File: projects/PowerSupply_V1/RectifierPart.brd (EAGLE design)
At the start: 80 x 45 mm, 12 parts, among them X1 IN, X2 PRI, X3 SEC, X4 OUT

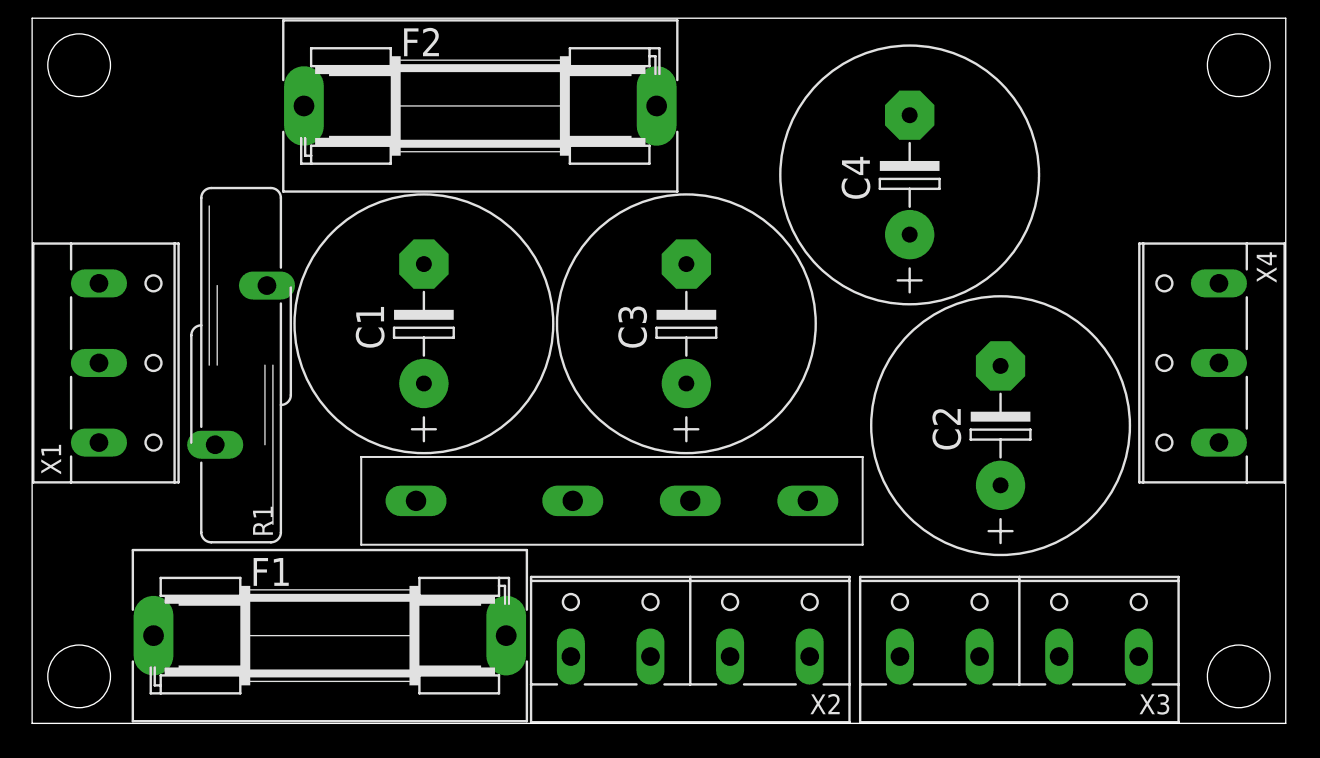
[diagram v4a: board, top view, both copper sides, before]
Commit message: feat: rectifier part routing finished
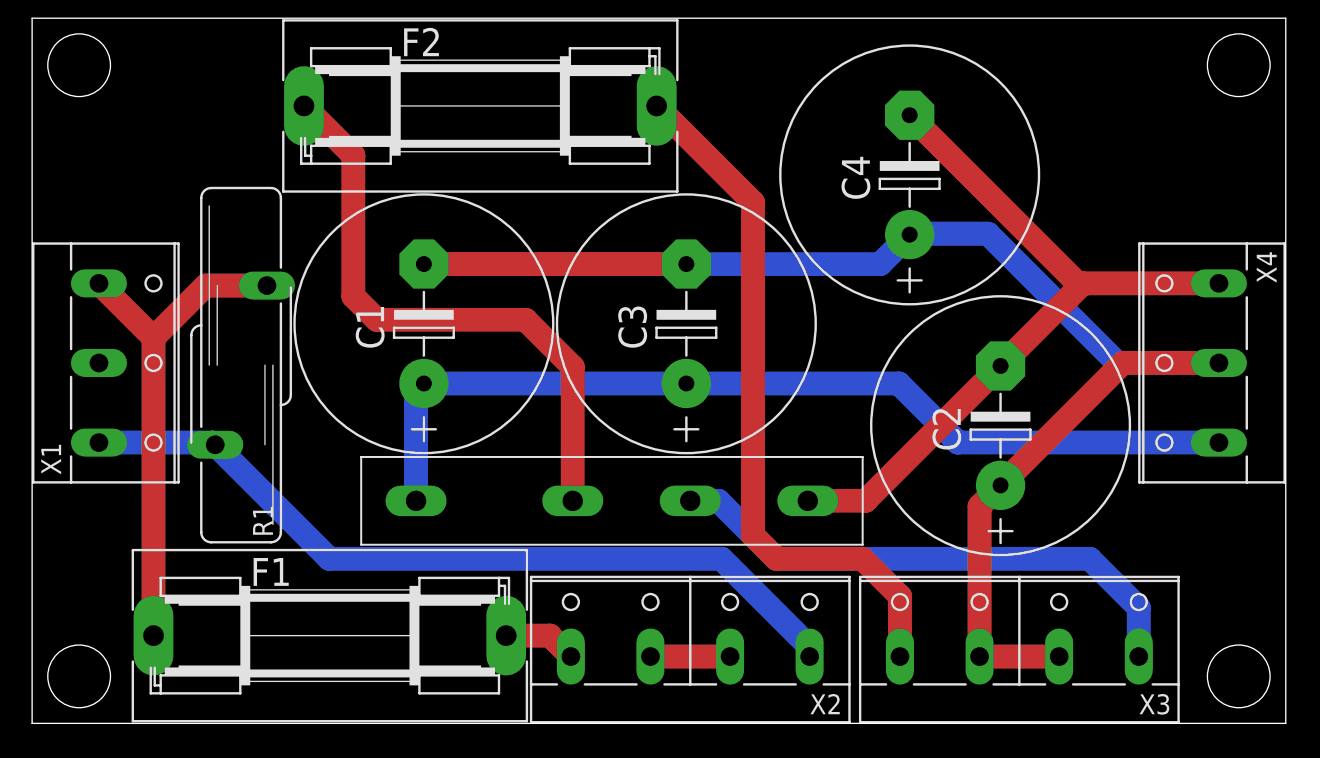
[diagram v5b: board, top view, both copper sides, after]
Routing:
- net GND: track 0.00 -> 88.7 mm
- net +20V: track 0.00 -> 60.0 mm
- net -230VAC: track 0.00 -> 51.4 mm
- net -20V: track 0.00 -> 47.5 mm
- net +15VAC: track 0.00 -> 44.8 mm
- net N$1: track 0.00 -> 37.9 mm
- net -15VAC: track 0.00 -> 34.6 mm
- net +230VAC: track 0.00 -> 32.5 mm
- net N$2: track 0.00 -> 5.08 mm
- net N$3: track 0.00 -> 4.68 mm
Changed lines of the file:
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@@
 <autorouter>
 <pass name="Default">
-<param name="RoutingGrid" value="50mil"/>
+<param name="RoutingGrid" value="0.125mm"/>
 <param name="AutoGrid" value="1"/>
-<param name="Efforts" value="0"/>
+<param name="Efforts" value="2"/>
 <param name="TopRouterVariant" value="1"/>
 <param name="tpViaShape" value="round"/>
-<param name="PrefDir.1" value="a"/>
+<param name="PrefDir.1" value="*"/>
 <param name="PrefDir.2" value="0"/>
 <param name="PrefDir.3" value="0"/>
@@
 <param name="PrefDir.14" value="0"/>
 <param name="PrefDir.15" value="0"/>
-<param name="PrefDir.16" value="a"/>
+<param name="PrefDir.16" value="-"/>
 <param name="cfVia" value="8"/>
 <param name="cfNonPref" value="5"/>
@@
 <contactref element="C3" pad="-"/>
 <contactref element="C2" pad="+"/>
+<contactref element="X4" pad="2"/>
+<wire x1="65.54" y1="4.265" x2="60.46" y2="4.265" width="1.524" layer="1"/>
+<wire x1="60.46" y1="4.265" x2="60.46" y2="13.85" width="1.524" layer="1"/>
+<wire x1="60.46" y1="13.85" x2="61.8" y2="15.19" width="1.524" layer="1"/>
+<wire x1="61.8" y1="15.19" x2="69.61" y2="23" width="1.524" layer="1"/>
+<wire x1="69.61" y1="23" x2="75.735" y2="23" width="1.524" layer="1"/>
+<wire x1="25" y1="29.31" x2="41.75" y2="29.31" width="1.524" layer="1"/>
 <contactref element="C1" pad="-"/>
-<contactref element="X4" pad="2"/>
+<contactref element="X3" pad="2"/>
 <contactref element="X3" pad="3"/>
-<contactref element="X3" pad="2"/>
-<wire x1="61.8" y1="15.19" x2="75.735" y2="23" width="0" layer="19" extent="1-1"/>
-<wire x1="60.46" y1="4.265" x2="61.8" y2="15.19" width="0" layer="19" extent="1-1"/>
-<wire x1="65.54" y1="4.265" x2="60.46" y2="4.265" width="0" layer="19" extent="1-1"/>
-<wire x1="56" y1="31.19" x2="61.8" y2="15.19" width="0" layer="19" extent="1-1"/>
-<wire x1="41.75" y1="29.31" x2="56" y2="31.19" width="0" layer="19" extent="1-1"/>
-<wire x1="25" y1="29.31" x2="41.75" y2="29.31" width="0" layer="19" extent="1-1"/>
+<wire x1="41.75" y1="29.31" x2="54.12" y2="29.31" width="1.524" layer="16"/>
+<wire x1="54.12" y1="29.31" x2="56" y2="31.19" width="1.524" layer="16"/>
+<wire x1="75.735" y1="23" x2="69.25" y2="23" width="1.524" layer="16"/>
+<wire x1="69.25" y1="23" x2="61" y2="31.25" width="1.524" layer="16"/>
+<wire x1="61" y1="31.25" x2="56.06" y2="31.25" width="1.524" layer="16"/>
+<wire x1="56.06" y1="31.25" x2="56" y2="31.19" width="1.524" layer="16"/>
 </signal>
 <signal name="PE">
@@
 <contactref element="X2" pad="2"/>
 <contactref element="X2" pad="3"/>
-<wire x1="39.46" y1="4.265" x2="44.54" y2="4.265" width="0" layer="19" extent="1-1"/>
+<wire x1="39.46" y1="4.265" x2="44.54" y2="4.265" width="1.524" layer="1"/>
 </signal>
 <signal name="N$3">
+<contactref element="F1" pad="1"/>
 <contactref element="X2" pad="1"/>
-<contactref element="F1" pad="1"/>
-<wire x1="30.2522" y1="5.6" x2="34.38" y2="4.265" width="0" layer="19" extent="1-1"/>
+<wire x1="30.2522" y1="5.6" x2="33.045" y2="5.6" width="1.524" layer="1"/>
+<wire x1="33.045" y1="5.6" x2="34.38" y2="4.265" width="1.524" layer="1"/>
 </signal>
 <signal name="+230VAC">
@@
 <contactref element="F1" pad="2"/>
 <contactref element="R1" pad="2"/>
-<wire x1="4.265" y1="28.08" x2="14.986" y2="27.94" width="0" layer="19" extent="1-1"/>
-<wire x1="7.7478" y1="5.6" x2="4.265" y2="28.08" width="0" layer="19" extent="1-1"/>
+<wire x1="7.7478" y1="5.6" x2="7.7478" y2="24.5972" width="1.524" layer="1"/>
+<wire x1="7.7478" y1="24.5972" x2="4.265" y2="28.08" width="1.524" layer="1"/>
+<wire x1="14.986" y1="27.94" x2="11.0906" y2="27.94" width="1.524" layer="1"/>
+<wire x1="11.0906" y1="27.94" x2="7.7478" y2="24.5972" width="1.524" layer="1"/>
 </signal>
 <signal name="-230VAC">
 <contactref element="X1" pad="3"/>
+<contactref element="R1" pad="1"/>
 <contactref element="X2" pad="4"/>
-<contactref element="R1" pad="1"/>
-<wire x1="11.684" y1="17.78" x2="49.62" y2="4.265" width="0" layer="19" extent="1-1"/>
-<wire x1="4.265" y1="17.92" x2="11.684" y2="17.78" width="0" layer="19" extent="1-1"/>
+<wire x1="4.265" y1="17.92" x2="11.544" y2="17.92" width="1.524" layer="16"/>
+<wire x1="11.544" y1="17.92" x2="11.684" y2="17.78" width="1.524" layer="16"/>
+<wire x1="11.684" y1="17.78" x2="18.964" y2="10.5" width="1.524" layer="16"/>
+<wire x1="18.964" y1="10.5" x2="44" y2="10.5" width="1.524" layer="16"/>
+<wire x1="44" y1="10.5" x2="49.62" y2="4.88" width="1.524" layer="16"/>
+<wire x1="49.62" y1="4.88" x2="49.62" y2="4.265" width="1.524" layer="16"/>
 </signal>
 <signal name="+15VAC">
+<contactref element="F2" pad="1"/>
+<wire x1="39.8522" y1="39.4" x2="46" y2="33.2522" width="1.524" layer="1"/>
+<wire x1="46" y1="33.2522" x2="46" y2="12" width="1.524" layer="1"/>
+<wire x1="46" y1="12" x2="47.5" y2="10.5" width="1.524" layer="1"/>
+<wire x1="47.5" y1="10.5" x2="53" y2="10.5" width="1.524" layer="1"/>
+<wire x1="53" y1="10.5" x2="55.38" y2="8.12" width="1.524" layer="1"/>
+<wire x1="55.38" y1="8.12" x2="55.38" y2="4.265" width="1.524" layer="1"/>
 <contactref element="X3" pad="1"/>
-<contactref element="F2" pad="1"/>
-<wire x1="55.38" y1="4.265" x2="39.8522" y2="39.4" width="0" layer="19" extent="1-1"/>
 </signal>
 <signal name="-15VAC">
+<contactref element="R+1" pad="~VAC2"/>
 <contactref element="X3" pad="4"/>
-<contactref element="R+1" pad="~VAC2"/>
-<wire x1="42" y1="14.2" x2="70.62" y2="4.265" width="0" layer="19" extent="1-1"/>
+<wire x1="42" y1="14.2" x2="43.8" y2="14.2" width="1.524" layer="16"/>
+<wire x1="43.8" y1="14.2" x2="47.5" y2="10.5" width="1.524" layer="16"/>
+<wire x1="47.5" y1="10.5" x2="67.5" y2="10.5" width="1.524" layer="16"/>
+<wire x1="67.5" y1="10.5" x2="70.62" y2="7.38" width="1.524" layer="16"/>
+<wire x1="70.62" y1="7.38" x2="70.62" y2="4.265" width="1.524" layer="16"/>
 </signal>
 <signal name="-20V">
@@
 <contactref element="C2" pad="-"/>
 <contactref element="R+1" pad="-VDC"/>
-<wire x1="61.8" y1="22.81" x2="75.735" y2="28.08" width="0" layer="19" extent="1-1"/>
-<wire x1="49.5" y1="14.2" x2="61.8" y2="22.81" width="0" layer="19" extent="1-1"/>
-<wire x1="56" y1="38.81" x2="61.8" y2="22.81" width="0" layer="19" extent="1-1"/>
+<wire x1="75.735" y1="28.08" x2="67.07" y2="28.08" width="1.524" layer="1"/>
+<wire x1="67.07" y1="28.08" x2="61.8" y2="22.81" width="1.524" layer="1"/>
+<wire x1="49.5" y1="14.2" x2="53.19" y2="14.2" width="1.524" layer="1"/>
+<wire x1="53.19" y1="14.2" x2="61.8" y2="22.81" width="1.524" layer="1"/>
+<wire x1="56" y1="38.81" x2="66.73" y2="28.08" width="1.524" layer="1"/>
+<wire x1="66.73" y1="28.08" x2="67.07" y2="28.08" width="1.524" layer="1"/>
 </signal>
 <signal name="+20V">
 <contactref element="X4" pad="1"/>
 <contactref element="C3" pad="+"/>
+<contactref element="R+1" pad="+VDC"/>
 <contactref element="C1" pad="+"/>
-<contactref element="R+1" pad="+VDC"/>
-<wire x1="41.75" y1="21.69" x2="75.735" y2="17.92" width="0" layer="19" extent="1-1"/>
-<wire x1="25" y1="21.69" x2="41.75" y2="21.69" width="0" layer="19" extent="1-1"/>
-<wire x1="24.5" y1="14.2" x2="25" y2="21.69" width="0" layer="19" extent="1-1"/>
+<wire x1="24.5" y1="14.2" x2="24.5" y2="21.19" width="1.524" layer="16"/>
+<wire x1="24.5" y1="21.19" x2="25" y2="21.69" width="1.524" layer="16"/>
+<wire x1="25" y1="21.69" x2="41.75" y2="21.69" width="1.524" layer="16"/>
+<wire x1="41.75" y1="21.69" x2="55.31" y2="21.69" width="1.524" layer="16"/>
+<wire x1="59.08" y1="17.92" x2="75.735" y2="17.92" width="1.524" layer="16"/>
+<wire x1="55.31" y1="21.69" x2="59.08" y2="17.92" width="1.524" layer="16"/>
 </signal>
 <signal name="N$1">
 <contactref element="F2" pad="2"/>
 <contactref element="R+1" pad="~VAC1"/>
-<wire x1="34.5" y1="14.2" x2="17.3478" y2="39.4" width="0" layer="19" extent="1-1"/>
+<wire x1="17.3478" y1="39.4" x2="20.5" y2="36.2478" width="1.524" layer="1"/>
+<wire x1="20.5" y1="36.2478" x2="20.5" y2="27.25" width="1.524" layer="1"/>
+<wire x1="20.5" y1="27.25" x2="22" y2="25.75" width="1.524" layer="1"/>
+<wire x1="22" y1="25.75" x2="31.5" y2="25.75" width="1.524" layer="1"/>
+<wire x1="31.5" y1="25.75" x2="34.5" y2="22.75" width="1.524" layer="1"/>
+<wire x1="34.5" y1="22.75" x2="34.5" y2="14.2" width="1.524" layer="1"/>
 </signal>
 </signals>
